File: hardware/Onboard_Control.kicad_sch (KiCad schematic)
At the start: 6 parts, among them J8001 Conn_01x04_Pin, SW8001 CK_KMS2xxG, SW8002 CK_KMS2xxG, SW8003 CK_KMS2xxG, SW8004 CK_KMS2xxG, SW8005 CK_KMS2xxG

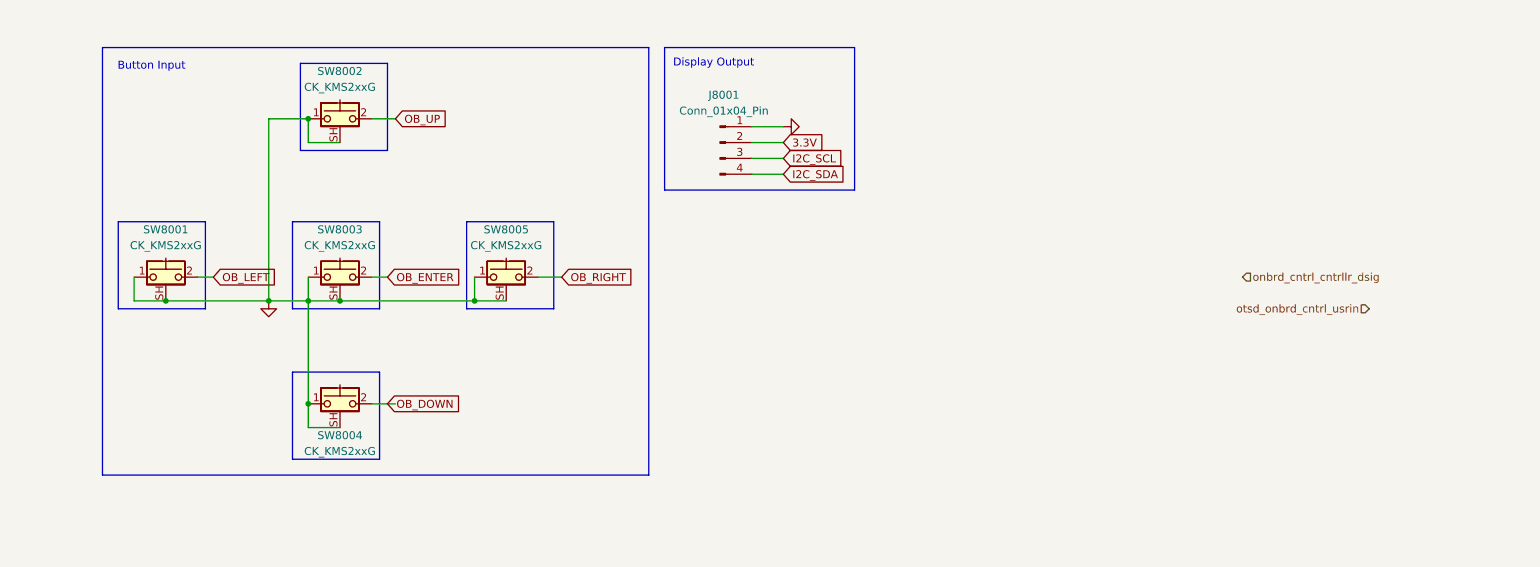
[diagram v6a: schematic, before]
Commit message: feat(PCB): fix all DRC errors
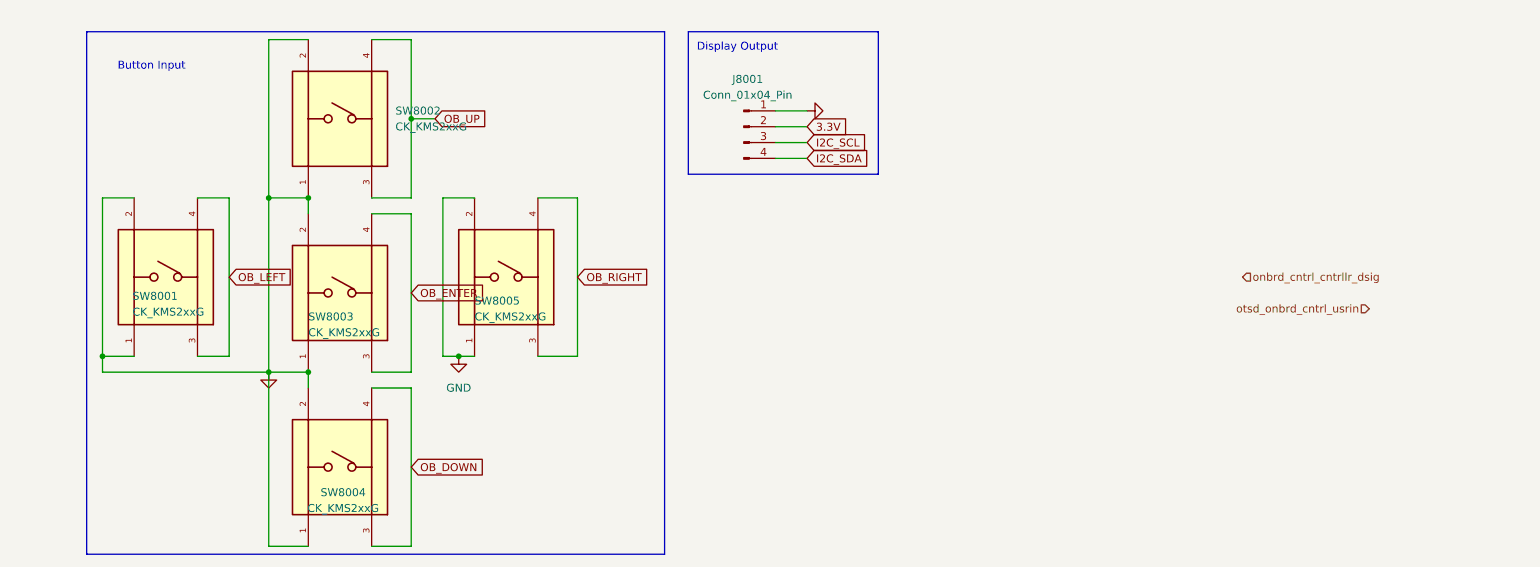
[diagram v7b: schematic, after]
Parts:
- SW8001, SW8002, SW8003, SW8004, SW8005: footprint Button_Switch_SMD:SW_SPST_CK_KMS2xxGP -> work:SW_TS02-66-70-BK-160-LCR-D; symbol Switch:CK_KMS2xxG -> Symbol_Library:TS02-66-70-BK-160-LCR-D; MANUFACTURER (none) -> CUI Devices; PARTREV (none) -> 1.0; STANDARD (none) -> Manufacturer Recommendations
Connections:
- net GND: now also SW8001.2, SW8002.2, SW8003.2, SW8004.2, SW8005.2; no longer SW8001.SH (B), SW8002.SH (B), SW8003.SH (B), SW8004.SH (B), SW8005.SH (B)
- net OB_DOWN: now also SW8004.3, SW8004.4; no longer SW8004.2
- net OB_ENTER: now also SW8003.3, SW8003.4; no longer SW8003.2
- net OB_LEFT: now also SW8001.3, SW8001.4; no longer SW8001.2
- net OB_RIGHT: now also SW8005.3, SW8005.4; no longer SW8005.2
- net OB_UP: now also SW8002.3, SW8002.4; no longer SW8002.2
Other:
- moved on the sheet: J8001

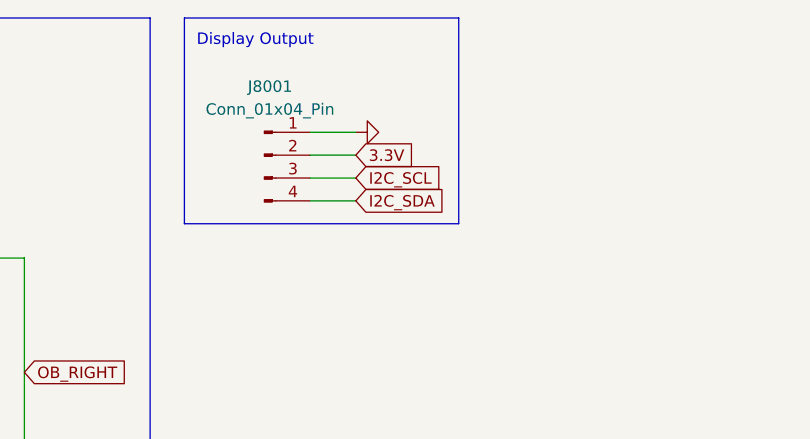
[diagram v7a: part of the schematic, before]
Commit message: feat(schematic): migrate to stm32f401re
Migrates to the stm32f401re in the schematic and pin mappings (for the
most part)
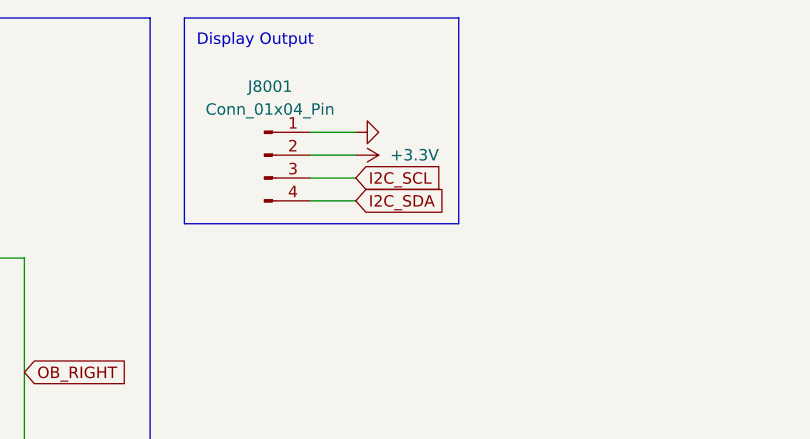
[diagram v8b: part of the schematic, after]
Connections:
- net 3.3V renamed +3.3V
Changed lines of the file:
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@@
-		)
-	)
-	(global_label "3.3V"
-		(shape input)
-		(at 139.7 78.74 0)
-		(fields_autoplaced yes)
-		(effects
-			(font
-				(size 1.27 1.27)
-			)
-			(justify left)
-		)
-		(property "Intersheetrefs" "${INTERSHEET_REFS}"
-			(at 146.7976 78.74 0)
-			(effects
-				(font
-					(size 1.27 1.27)
-				)
-				(justify left)
-				(hide yes)
-			)
 		)
 	)
@@
 		(shape input)
 		(at 209.55 102.87 0)
-		(fields_autoplaced yes)
 		(effects
 			(font
@@
 		(shape input)
 		(at 229.87 107.95 180)
-		(fields_autoplaced yes)
 		(effects
 			(font
@@
 					(unit 1)
 				)
+			)
+		)
+	)
+	(symbol
+		(lib_id "power:+3.3V")
+		(at 139.7 78.74 270)
+		(unit 1)
+		(exclude_from_sim no)
+		(in_bom yes)
+		(on_board yes)
+		(dnp no)
+		(fields_autoplaced yes)
+		(property "Reference" "#PWR08003"
+			(at 135.89 78.74 0)
+			(effects
+				(font
+					(size 1.27 1.27)
+				)
+				(hide yes)
+			)
+		)
+		(property "Value" "+3.3V"
+			(at 143.51 78.7399 90)
+			(effects
+				(font
+					(size 1.27 1.27)
+				)
+				(justify left)
+			)
+		)
+		(property "Footprint" ""
+			(at 139.7 78.74 0)
+			(effects
+				(font
+					(size 1.27 1.27)
+				)
+				(hide yes)
+			)
+		)
+		(property "Datasheet" ""
+			(at 139.7 78.74 0)
+			(effects
+				(font
+					(size 1.27 1.27)
+				)
+				(hide yes)
+			)
+		)
+		(property "Description" "Power symbol creates a global label with name \"+3.3V\""
+			(at 139.7 78.74 0)
+			(effects
+				(font
+					(size 1.27 1.27)
+				)
+				(hide yes)
+			)
+		)
+		(pin "1"
+		)
+		(instances
+			(project ""
+				(path "/d5303413-7068-41ba-88e3-39dfa38d31b7/5068f4fb-295f-4c02-a1ca-8a4133aa46e7"
+					(reference "#PWR08003")
+					(unit 1)
+				)
